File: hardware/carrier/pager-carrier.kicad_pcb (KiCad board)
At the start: 2 copper layers, 38.9 x 50 mm, 82 parts, among them J1 PANEL, J2 CARDKB, J3 HAPTIC, J4 EXT_LED, J5 PIEZ, J6 USB4235, J7 BATTERY, J8 FRONTLIGHT, M1 Walter, Q1 UMH3N, Q2 SI1308EDL, Q3 MMST3904, Q4 AO3401A, SW1 KMR221GLFS, SW2 JS102011SAQN, U1 CP2102N-A02-GQFN24, U2 SN74LVC2G126DCUR, U3 DRV2605LDGSR, U4 LIS2DW12TR, U5 BQ25185DLHR, U6 MAX17048G+T10, U7 TPS62840DLCR

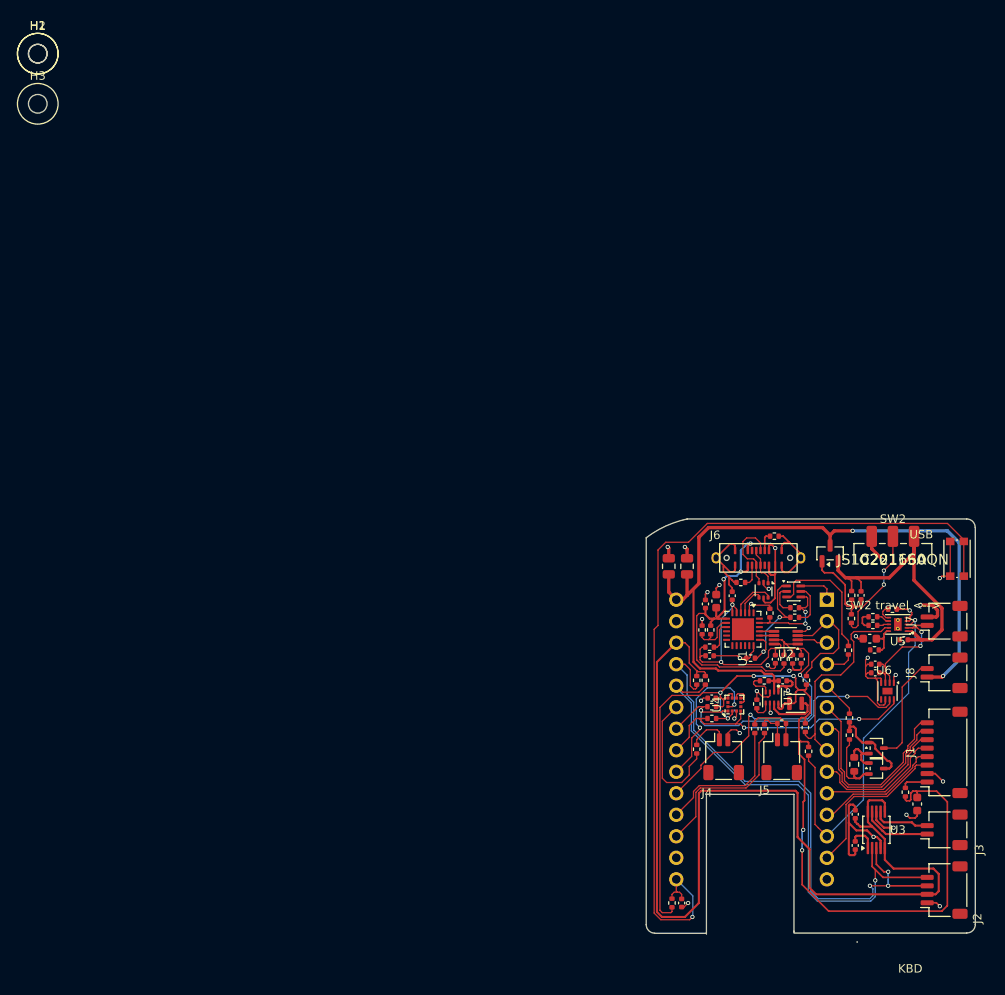
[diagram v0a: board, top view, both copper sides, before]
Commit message: Carrier: close the outline, tidy silkscreen, add GND pours (DRC 278 -> 28)
- Edge.Cuts rebuilt as a single closed loop (right edge 113.15, SIM notch, 1 mm corners)
- 0402/LGA parts moved to pager-carrier:*_NoSilk footprints (library copies without the
  silk outline), schematic fields updated; J6 silk box stops short of the shield pads;
  reference text re-placed or hidden; stale board texts removed
- GND pours both layers (0.2 clearance, thermal reliefs), 3 stitching vias for the
  top-side GND groups that had no path to the plane; all GND connected
- Remaining: 4 owner routing clearances, H1-H3 parked off-board, 2 unrouted nets

Co-Authored-By: Claude Fable 5.1 <noreply@anthropic.com>
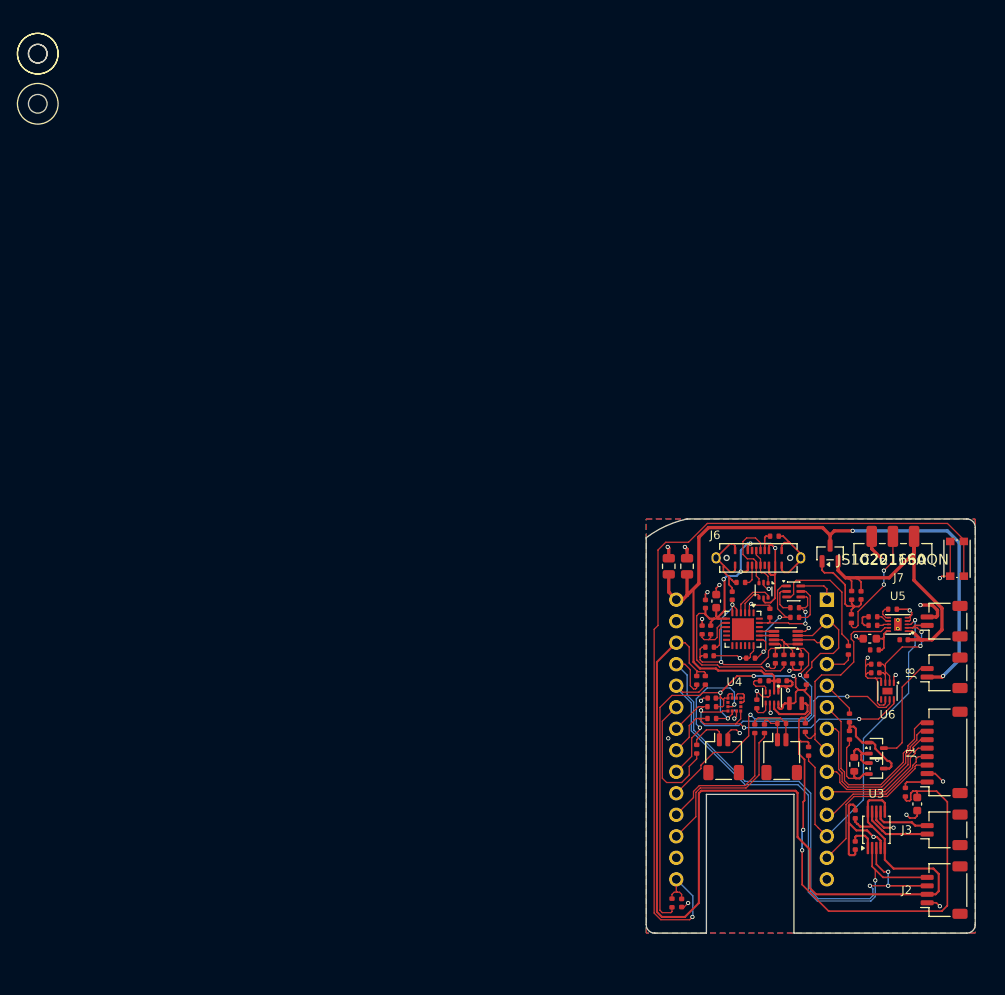
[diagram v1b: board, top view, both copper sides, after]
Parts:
- C10, C11, C12, C14, C15, C16, C17, C18, C19, C2, C3, C4, C5, C9: footprint Capacitor_SMD:C_0402_1005Metric -> pager-carrier:C_0402_1005Metric_NoSilk
- L1: footprint Inductor_SMD:L_Murata_DFE201610P -> pager-carrier:L_Murata_DFE201610P_NoSilk
- R1, R10, R11, R14, R15, R16, R17, R18, R19, R2, R20, R21, R22, R23, R24, R25, R26, R27, R28, R29, R3, R30, R31, R32, R33, R34, R37, R38, R39, R4, R5, R6, R7, R8, R9: footprint Resistor_SMD:R_0402_1005Metric -> pager-carrier:R_0402_1005Metric_NoSilk
- U4: footprint Package_LGA:LGA-12_2x2mm_P0.5mm -> pager-carrier:LGA-12_2x2mm_P0.5mm_NoSilk
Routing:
- net GND: vias 30 -> 32
- added copper zone on B.Cu, net GND
- added copper zone on F.Cu, net GND
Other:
- board size 38.9 x 50 mm -> 38.9 x 48.9 mm
- board text removed: "KBD"
- board text removed: "SW2 travel <-->"
- board text removed: "USB"
